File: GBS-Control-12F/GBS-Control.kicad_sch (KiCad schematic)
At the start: 16 parts, among them J1 PROG, U1 PLCC-44 socket, U2 ESP-12F

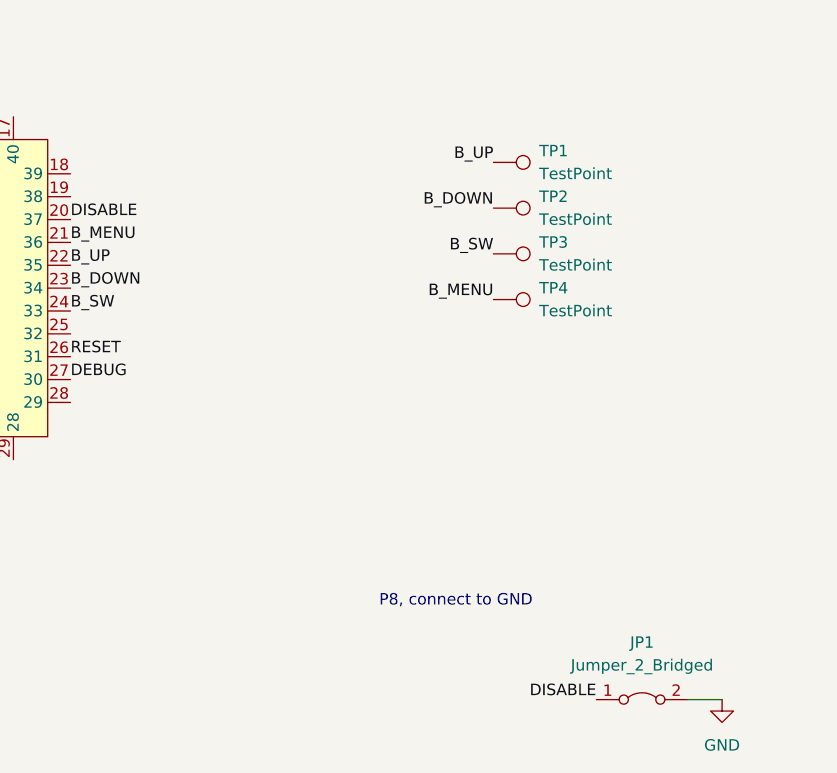
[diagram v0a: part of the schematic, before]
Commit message: KiCAD : add a port to connect the Si5351 Clock Generator
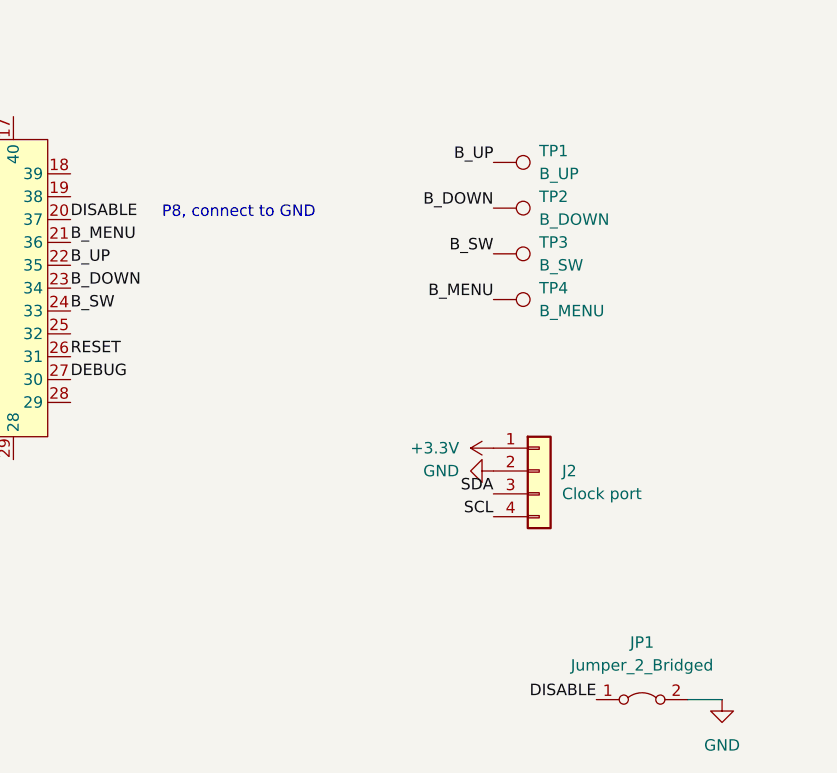
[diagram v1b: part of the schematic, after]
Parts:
- added J2: Clock port, Connector_PinHeader_2.54mm:PinHeader_1x04_P2.54mm_Vertical, symbol Connector_Generic:Conn_01x04
- TP1: value TestPoint -> B_UP
- TP2: value TestPoint -> B_DOWN
- TP3: value TestPoint -> B_SW
- TP4: value TestPoint -> B_MENU
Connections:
- net +3.3V: now also J2.1 (Pin_1)
- net GND: now also J2.2 (Pin_2)
- net SCL: now also J2.4 (Pin_4)
- net SDA: now also J2.3 (Pin_3)
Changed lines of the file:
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@@
     (effects (font (size 1.27 1.27)) (justify left bottom))
   )
-  (text "P8, connect to GND" (at 140.97 133.35 0)
+  (text "P8, connect to GND" (at 116.84 90.17 0)
     (effects (font (size 1.27 1.27)) (justify left bottom))
   )
@@
     (effects (font (size 1.27 1.27)) (justify right bottom))
   )
+  (label "SCL" (at 153.67 123.19 180)
+    (effects (font (size 1.27 1.27)) (justify right bottom))
+  )
   (label "B_DOWN" (at 153.67 88.9 180)
     (effects (font (size 1.27 1.27)) (justify right bottom))
@@
     (effects (font (size 1.27 1.27)) (justify left bottom))
   )
+  (label "SDA" (at 153.67 120.65 180)
+    (effects (font (size 1.27 1.27)) (justify right bottom))
+  )
   (label "GPIO2" (at 227.33 87.63 0)
     (effects (font (size 1.27 1.27)) (justify left bottom))
@@
   (label "GPIO0" (at 256.54 105.41 180)
     (effects (font (size 1.27 1.27)) (justify right bottom))
+  )
+  (symbol (lib_id "power:+3.3V") (at 153.67 115.57 90) (unit 1)
+    (in_bom yes) (on_board yes) (fields_autoplaced)
+    (property "Reference" "#PWR013" (id 0) (at 157.48 115.57 0)
+      (effects (font (size 1.27 1.27)) hide)
+    )
+    (property "Value" "+3.3V" (id 1) (at 149.86 115.5699 90)
+      (effects (font (size 1.27 1.27)) (justify left))
+    )
+    (property "Footprint" "" (id 2) (at 153.67 115.57 0)
+      (effects (font (size 1.27 1.27)) hide)
+    )
+    (property "Datasheet" "" (id 3) (at 153.67 115.57 0)
+      (effects (font (size 1.27 1.27)) hide)
+    )
+    (pin "1")
   )
   (symbol (lib_id "power:GND") (at 195.58 57.15 0) (unit 1)
@@
     )
     (property "Datasheet" "" (id 3) (at 261.62 72.39 0)
+      (effects (font (size 1.27 1.27)) hide)
+    )
+    (pin "1")
+  )
+  (symbol (lib_id "power:GND") (at 153.67 118.11 270) (unit 1)
+    (in_bom yes) (on_board yes) (fields_autoplaced)
+    (property "Reference" "#PWR014" (id 0) (at 147.32 118.11 0)
+      (effects (font (size 1.27 1.27)) hide)
+    )
+    (property "Value" "GND" (id 1) (at 149.86 118.1099 90)
+      (effects (font (size 1.27 1.27)) (justify right))
+    )
+    (property "Footprint" "" (id 2) (at 153.67 118.11 0)
+      (effects (font (size 1.27 1.27)) hide)
+    )
+    (property "Datasheet" "" (id 3) (at 153.67 118.11 0)
       (effects (font (size 1.27 1.27)) hide)
     )
@@
       (effects (font (size 1.27 1.27)) (justify left))
     )
-    (property "Value" "TestPoint" (id 1) (at 158.75 95.2499 90)
+    (property "Value" "B_SW" (id 1) (at 158.75 95.2499 90)
       (effects (font (size 1.27 1.27)) (justify left))
     )
@@
       (effects (font (size 1.27 1.27)) (justify left))
     )
-    (property "Value" "TestPoint" (id 1) (at 158.75 100.3299 90)
+    (property "Value" "B_MENU" (id 1) (at 158.75 100.3299 90)
       (effects (font (size 1.27 1.27)) (justify left))
     )
@@
       (effects (font (size 1.27 1.27)) (justify left))
     )
-    (property "Value" "TestPoint" (id 1) (at 158.75 85.0899 90)
+    (property "Value" "B_UP" (id 1) (at 158.75 85.0899 90)
       (effects (font (size 1.27 1.27)) (justify left))
     )
@@
       (effects (font (size 1.27 1.27)) (justify left))
     )
-    (property "Value" "TestPoint" (id 1) (at 158.75 90.1699 90)
+    (property "Value" "B_DOWN" (id 1) (at 158.75 90.1699 90)
       (effects (font (size 1.27 1.27)) (justify left))
     )
@@
     )
     (pin "1")
+  )
+  (symbol (lib_id "Connector_Generic:Conn_01x04") (at 158.75 118.11 0) (unit 1)
+    (in_bom yes) (on_board yes) (fields_autoplaced)
+    (property "Reference" "J2" (id 0) (at 161.29 118.1099 0)
+      (effects (font (size 1.27 1.27)) (justify left))
+    )
+    (property "Value" "Clock port" (id 1) (at 161.29 120.6499 0)
+      (effects (font (size 1.27 1.27)) (justify left))
+    )
+    (property "Footprint" "Connector_PinHeader_2.54mm:PinHeader_1x04_P2.54mm_Vertical" (id 2) (at 158.75 118.11 0)
+      (effects (font (size 1.27 1.27)) hide)
+    )
+    (property "Datasheet" "~" (id 3) (at 158.75 118.11 0)
+      (effects (font (size 1.27 1.27)) hide)
+    )
+    (pin "1")
+    (pin "2")
+    (pin "3")
+    (pin "4")
   )
   (symbol (lib_id "Device:C_Small") (at 261.62 80.01 0) (unit 1)
@@
       (reference "#PWR012") (unit 1) (value "+3.3V") (footprint "")
     )
+    (path "/028593a2-c89b-4933-8908-cb54ed6ec345"
+      (reference "#PWR013") (unit 1) (value "+3.3V") (footprint "")
+    )
+    (path "/2aa3811e-c8de-45da-8461-a4d90f92ca82"
+      (reference "#PWR014") (unit 1) (value "GND") (footprint "")
+    )
     (path "/de315ed7-c989-4a04-a0b0-f4d9be38c2a0"
       (reference "#PWR0101") (unit 1) (value "+3.3V") (footprint "")
@@
       (reference "J1") (unit 1) (value "PROG") (footprint "Connector_PinSocket_2.54mm:PinSocket_1x06_P2.54mm_Vertical")
     )
+    (path "/e030e3d0-2739-47f1-8be4-414cddeb8720"
+      (reference "J2") (unit 1) (value "Clock port") (footprint "Connector_PinHeader_2.54mm:PinHeader_1x04_P2.54mm_Vertical")
+    )
     (path "/54c5d063-2856-40e7-ba64-3c2e09206442"
       (reference "JP1") (unit 1) (value "Jumper_2_Bridged") (footprint "Jumper:SolderJumper-2_P1.3mm_Bridged_RoundedPad1.0x1.5mm")
@@
     )
     (path "/8149fce5-4fda-4cd4-ab06-9871c543f3b2"
-      (reference "TP1") (unit 1) (value "TestPoint") (footprint "TestPoint:TestPoint_Pad_D1.0mm")
+      (reference "TP1") (unit 1) (value "B_UP") (footprint "TestPoint:TestPoint_Pad_D1.0mm")
     )
     (path "/a1bf0537-268e-4aa1-af66-208fb1c2b91e"
-      (reference "TP2") (unit 1) (value "TestPoint") (footprint "TestPoint:TestPoint_Pad_D1.0mm")
+      (reference "TP2") (unit 1) (value "B_DOWN") (footprint "TestPoint:TestPoint_Pad_D1.0mm")
     )
     (path "/6ae9ad32-9046-4e28-8e2d-0c83d44b6a60"
-      (reference "TP3") (unit 1) (value "TestPoint") (footprint "TestPoint:TestPoint_Pad_D1.0mm")
+      (reference "TP3") (unit 1) (value "B_SW") (footprint "TestPoint:TestPoint_Pad_D1.0mm")
     )
     (path "/75786f28-9319-41a4-8477-421d6fa968d3"
-      (reference "TP4") (unit 1) (value "TestPoint") (footprint "TestPoint:TestPoint_Pad_D1.0mm")
+      (reference "TP4") (unit 1) (value "B_MENU") (footprint "TestPoint:TestPoint_Pad_D1.0mm")
     )
     (path "/f402a2e4-184a-49e9-9b5a-85c4ce735b3e"

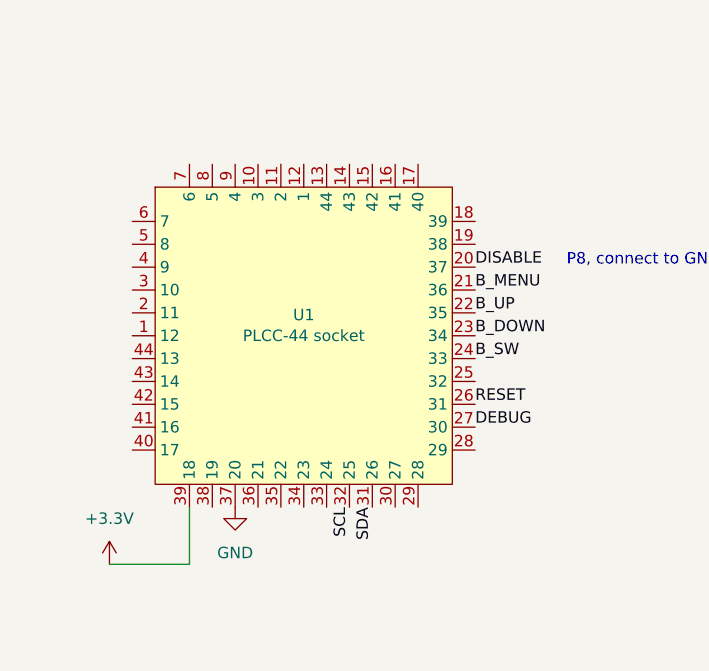
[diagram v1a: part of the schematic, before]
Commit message: GBS-Control-12F, GBS-Control-M2 : update socket symbol and footprint, no PCB change
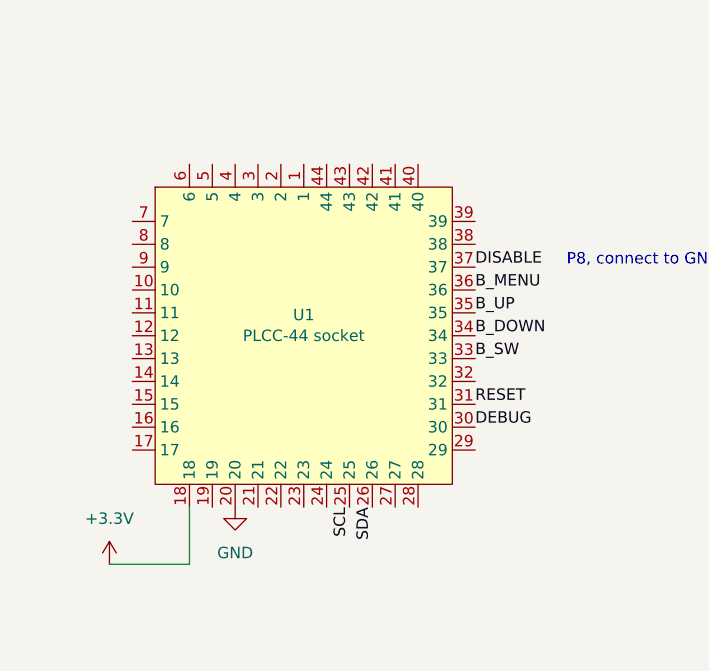
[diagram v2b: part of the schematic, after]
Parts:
- U1: footprint Package_LCC:PLCC-44_THT-Socket -> Sassa:PLCC-44_THT-SocketOnTop; symbol Sassa:PLCC-44_Socket-on-top -> Sassa:PLCC-44
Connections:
- net +3.3V: now also U1.18; no longer U1.39 (18)
- net B_DOWN: now also U1.34; no longer U1.23 (34)
- net B_MENU: now also U1.36; no longer U1.21 (36)
- net B_SW: now also U1.33; no longer U1.24 (33)
- net B_UP: now also U1.35; no longer U1.22 (35)
- net DEBUG: now also U1.30; no longer U1.27 (30)
- net DISABLE: now also U1.37; no longer U1.20 (37)
- net GND: now also U1.20; no longer U1.37 (20)
- net RESET: now also U1.31; no longer U1.26 (31)
- net SCL: now also U1.25; no longer U1.32 (25)
- net SDA: now also U1.26; no longer U1.31 (26)
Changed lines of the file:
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@@
     (pin "1")
   )
-  (symbol (lib_id "Sassa:PLCC-44_Socket-on-top") (at 87.63 97.79 0) (unit 1)
+  (symbol (lib_id "Sassa:PLCC-44") (at 87.63 97.79 0) (unit 1)
     (in_bom yes) (on_board yes)
     (property "Reference" "U1" (id 0) (at 87.63 95.4786 0))
     (property "Value" "PLCC-44 socket" (id 1) (at 87.63 97.79 0))
-    (property "Footprint" "Package_LCC:PLCC-44_THT-Socket" (id 2) (at 87.63 97.79 0)
+    (property "Footprint" "Sassa:PLCC-44_THT-SocketOnTop" (id 2) (at 87.63 97.79 0)
       (effects (font (size 1.27 1.27)) hide)
     )
@@
     )
     (path "/f402a2e4-184a-49e9-9b5a-85c4ce735b3e"
-      (reference "U1") (unit 1) (value "PLCC-44 socket") (footprint "Package_LCC:PLCC-44_THT-Socket")
+      (reference "U1") (unit 1) (value "PLCC-44 socket") (footprint "Sassa:PLCC-44_THT-SocketOnTop")
     )
     (path "/f14c3704-a74d-4015-9db4-db9e84a7a10e"

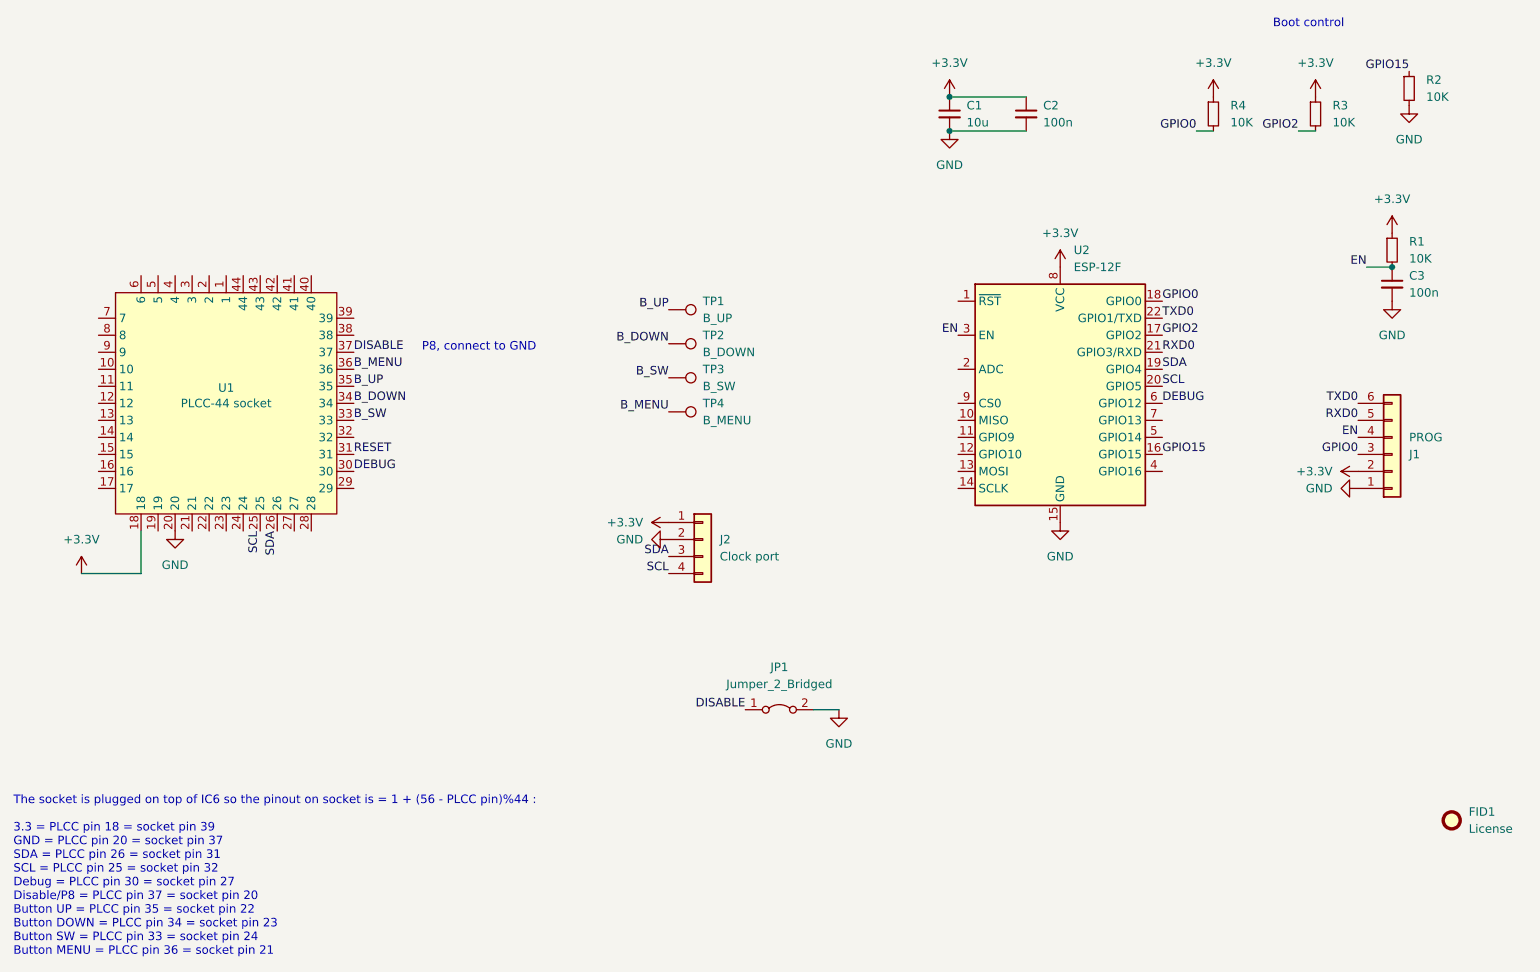
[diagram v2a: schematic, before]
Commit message: GBS-Control-12F, GBS-Control-M2 : update ibom ; small silkscreen change
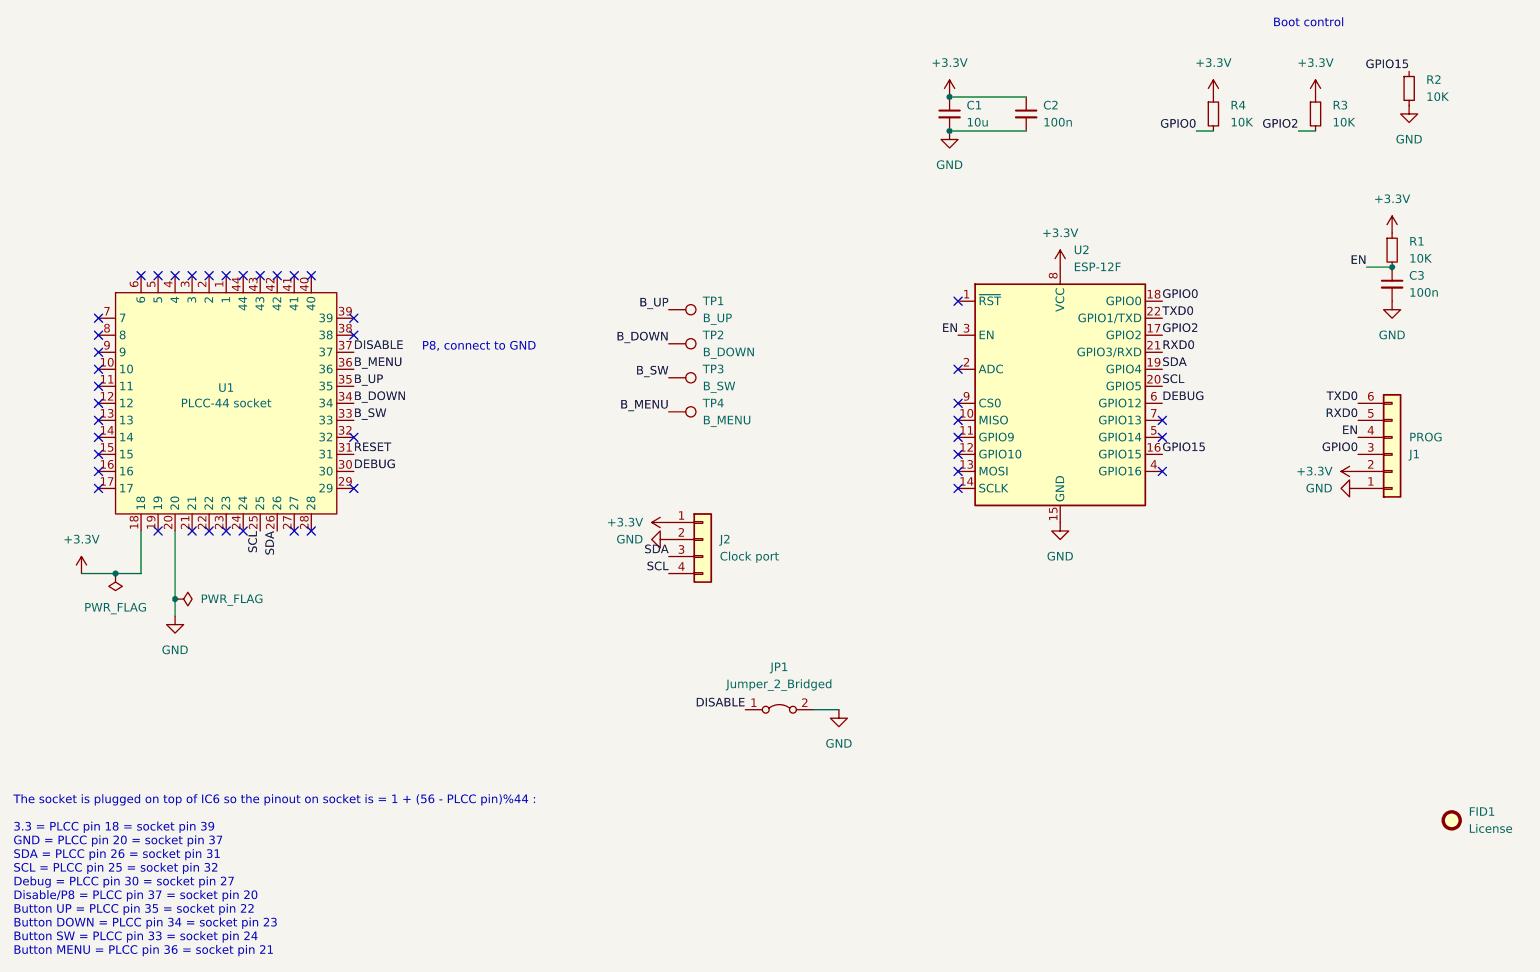
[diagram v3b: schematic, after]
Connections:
- no-connect marks 0 -> 44
